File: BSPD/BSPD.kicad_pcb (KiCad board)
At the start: 4 copper layers, 53.3 x 27.9 mm, 72 parts, among them J1 Signal, J2 Power, Q1 2N7002, Q2 BSS84, Q3 2N7002, Q4 2N7002, Q5 2N7002, Q6 2N7002, U1 LM339, U2 LM339

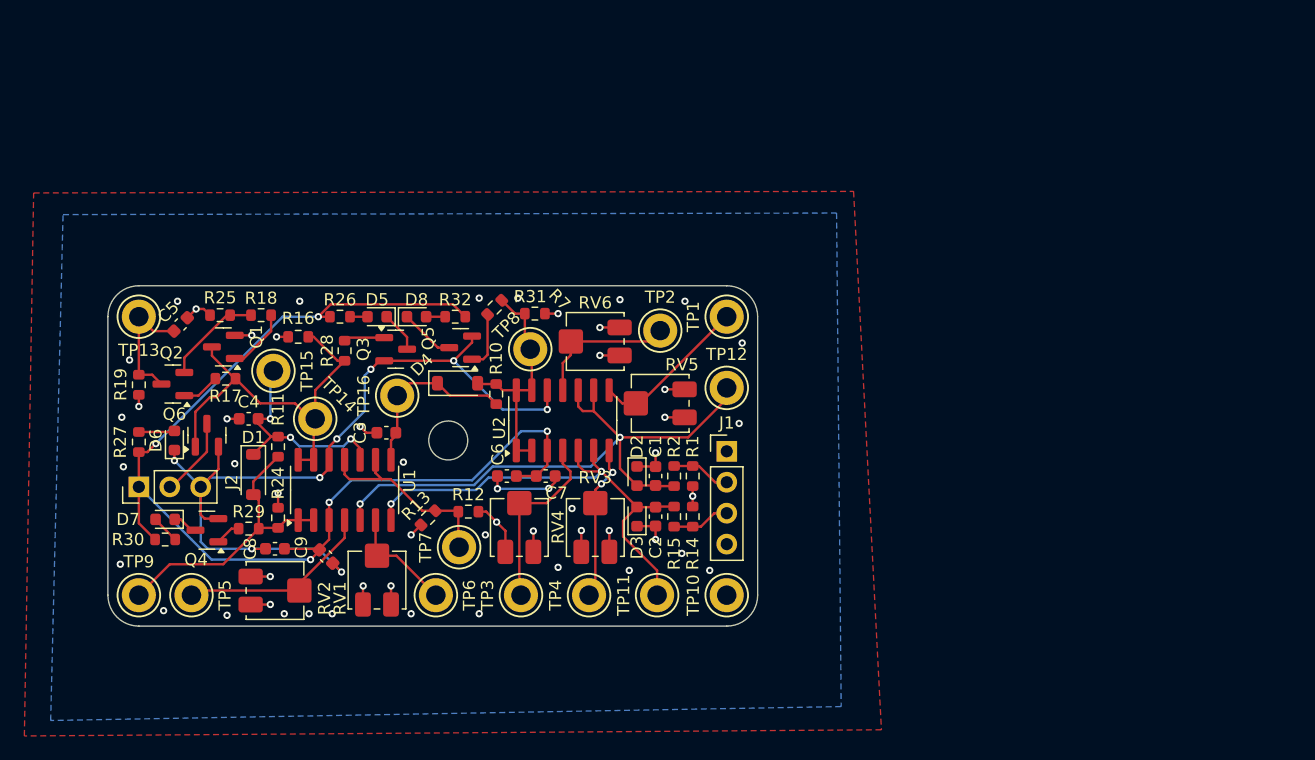
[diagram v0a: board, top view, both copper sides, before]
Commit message: feat: begin rev b
- Change parts to reduce cost (remove extended components)
- Reset PCB to prep layout
- Switch to resistor dividers
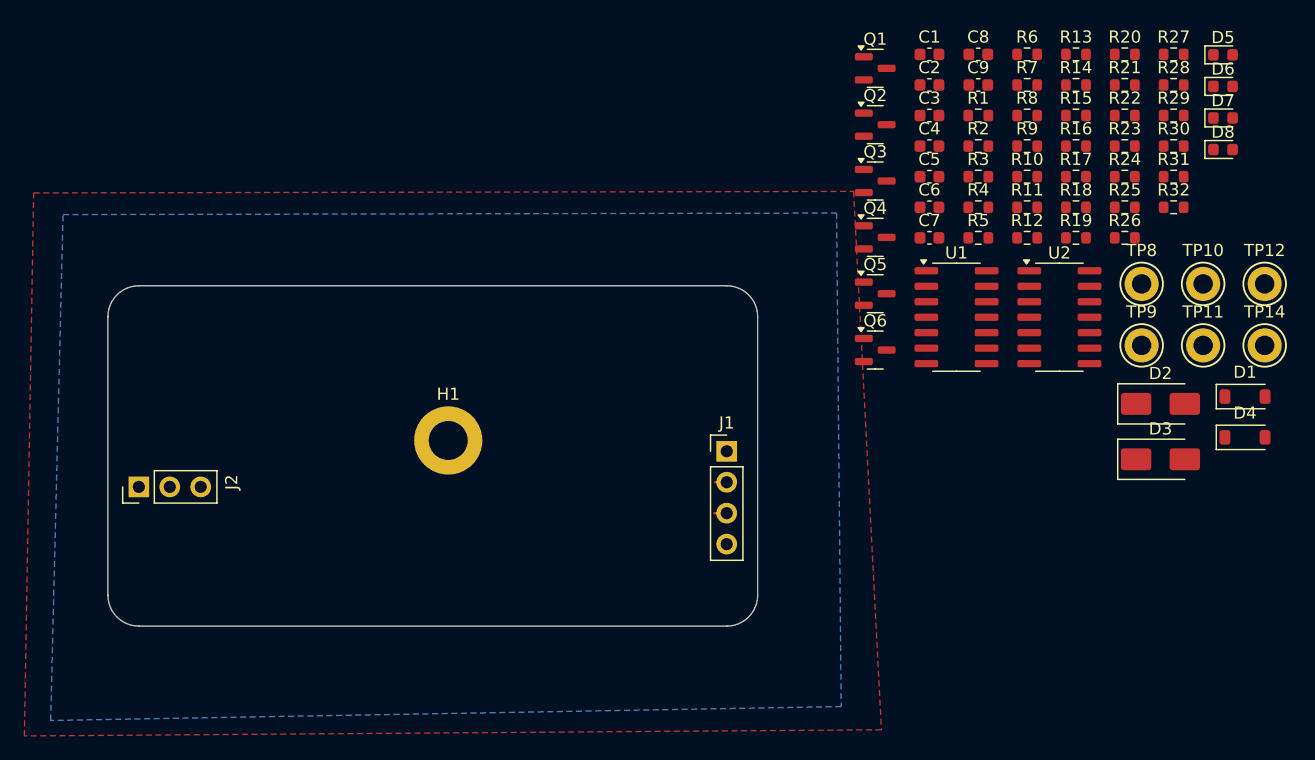
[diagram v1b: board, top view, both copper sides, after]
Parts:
- removed RV1, RV2, RV3, RV4, RV5, RV6: 3314J-1-103E, Potentiometer_SMD:Potentiometer_Bourns_3314J_Vertical
- removed TP1: TPS OV, TestPoint:TestPoint_Keystone_5005-5009_Compact
- removed TP13: Latching RC, TestPoint:TestPoint_Keystone_5005-5009_Compact
- removed TP15: ~{PANIC BRAKE} RC, TestPoint:TestPoint_Keystone_5005-5009_Compact
- removed TP16: SENSORS_OK RC, TestPoint:TestPoint_Keystone_5005-5009_Compact
- removed TP2: TPS UV, TestPoint:TestPoint_Keystone_5005-5009_Compact
- removed TP3: BPT OV, TestPoint:TestPoint_Keystone_5005-5009_Compact
- removed TP4: BPT UV, TestPoint:TestPoint_Keystone_5005-5009_Compact
- removed TP5: TPS 10%, TestPoint:TestPoint_Keystone_5005-5009_Compact
- removed TP6: BPT HB, TestPoint:TestPoint_Keystone_5005-5009_Compact
- removed TP7: TAU, TestPoint:TestPoint_Keystone_5005-5009_Compact
- added R20: 100K, Resistor_SMD:R_0603_1608Metric, F.Cu at (157.1, 29.3)
- added R21: 100K, Resistor_SMD:R_0603_1608Metric, F.Cu at (157.1, 31.8)
- added R22: 100K, Resistor_SMD:R_0603_1608Metric, F.Cu at (157.1, 34.3)
- added R23: 100K, Resistor_SMD:R_0603_1608Metric, F.Cu at (157.1, 36.8)
- added R3: 10K, Resistor_SMD:R_0603_1608Metric, F.Cu at (145.1, 39.3)
- added R4: 100K, Resistor_SMD:R_0603_1608Metric, F.Cu at (145.1, 41.8)
- added R5: 100K, Resistor_SMD:R_0603_1608Metric, F.Cu at (145.1, 44.3)
- added R6: 100K, Resistor_SMD:R_0603_1608Metric, F.Cu at (149.1, 29.3)
- added R8: 100K, Resistor_SMD:R_0603_1608Metric, F.Cu at (149.1, 34.3)
- added R9: 100K, Resistor_SMD:R_0603_1608Metric, F.Cu at (149.1, 36.8)
- C1, C2: value 150nF -> 220nF
- D1, D4: value BAT43W-V -> RB160M-30
- D2, D3: value ESDA-05N -> SMAJ5.0A; footprint Diode_SMD:D_0603_1608Metric -> Diode_SMD:D_SMA
- H1: value MountingHole -> MountingHole_Pad; footprint MountingHole:MountingHole_3.2mm_M3 -> MountingHole:MountingHole_3.2mm_M3_DIN965_Pad
- Q2: value BSS84 -> AO3401A
- R10: value 10K -> 100K
- TP9: value ~{PANIC BRAKE} -> PANIC BRAKE
- moved D7 92.9 mm to (165.2, 34.5), turned to 0 degrees
- moved D6 90.9 mm to (165.2, 31.9), turned to 0 degrees
- moved R27 90.7 mm to (161.2, 29.3), turned to 0 degrees
- moved R30 88.9 mm to (161.2, 36.8), turned to 0 degrees
- moved TP9 84.8 mm to (158.5, 53.2)
- moved R29 83.2 mm to (161.2, 34.3), turned to 0 degrees
- moved D1 81.7 mm to (167.0, 57.4), turned to 0 degrees
- moved TP14 78.2 mm to (168.6, 53.2), turned to 0 degrees
- moved R19 77.9 mm to (153.1, 44.3), turned to 0 degrees
- moved R24 74.9 mm to (157.1, 39.3), turned to 0 degrees
- moved R25 74.8 mm to (157.1, 41.8)
- moved D5 72.7 mm to (165.2, 29.3), turned to 0 degrees
- moved R17 71.8 mm to (153.1, 39.3), turned to 0 degrees
- moved R28 71.5 mm to (161.2, 31.8), turned to 0 degrees
- moved C8 70.6 mm to (145.1, 29.3), turned to 0 degrees
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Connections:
- C4 pad 1: Net-(D1-K) -> Net-(D1-A)
- C5 pad 1: Net-(Q2-D) -> Net-(Q2-S)
- D1 pad 1: Net-(D1-K) -> /PANIC_BRAKE
- D1 pad 2: /~{PANIC_BRAKE} -> Net-(D1-A)
- D2 pad 1: GNDA -> /BPT_SIG
- D2 pad 2: /TPS -> GNDA
- D3 pad 1: GNDA -> /TPS_SIG
- D3 pad 2: /BPT -> GNDA
- R10 pad 1: /SENSORS_OK -> Net-(U2A--)
- R10 pad 2: Net-(D4-K) -> GNDA
- R11 pad 1: /~{PANIC_BRAKE} -> /PANIC_BRAKE
- R11 pad 2: Net-(D1-K) -> Net-(D1-A)
- R18 pad 2: Net-(Q2-S) -> Net-(Q2-D)
- R19 pad 1: Net-(Q2-D) -> Net-(Q2-S)
- R24 pad 1: /~{PANIC_BRAKE} -> /PANIC_BRAKE
- R25 pad 2: Net-(Q2-S) -> Net-(Q2-D)
- TP9 pad 1: /~{PANIC_BRAKE} -> /PANIC_BRAKE
- U1 pad 1: /~{PANIC_BRAKE} -> /PANIC_BRAKE
- U1 pad 10: Net-(D1-K) -> Net-(D1-A)
- U1 pad 2: /~{PANIC_BRAKE} -> /PANIC_BRAKE
- U1 pad 8: Net-(D4-K) -> /1_RC
- U1 pad 9: /1_RC -> Net-(D4-K)
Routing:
- net +BATT: track 91.7 -> 0.00 mm, vias 5 -> 0
- net -BATT: track 85.7 -> 0.00 mm, vias 10 -> 0
- net /TPS: track 51.0 -> 0.00 mm, vias 2 -> 0
- net /BPT: track 41.1 -> 0.00 mm, vias 2 -> 0
- net /BSPD_OK: track 32.9 -> 0.00 mm
- net GNDA: track 26.0 -> 0.00 mm, vias 40 -> 0
- net /~{PANIC_BRAKE}: track 23.8 -> 0.00 mm
- net /SENSORS_OK: track 19.8 -> 0.00 mm
- net Net-(D1-K): track 19.5 -> 0.00 mm, vias 3 -> 0
- net /1_RC: track 16.5 -> 0.00 mm
- net Net-(U1A--): track 16.3 -> 0.00 mm
- net +5VA: track 16.0 -> 0.00 mm, vias 11 -> 0
- net Net-(U2A--): track 15.2 -> 0.00 mm
- net Net-(D4-K): track 14.7 -> 0.00 mm
- net Net-(U2D--): track 13.0 -> 0.00 mm
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
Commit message: BSPD rev 2a
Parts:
- removed D2, D3: SMAJ5.0A, Diode_SMD:D_SMA
- removed D6, D7, D8: LED, LED_SMD:LED_0603_1608Metric
- removed H1: MountingHole_Pad, MountingHole:MountingHole_3.2mm_M3_DIN965_Pad
- removed Q3, Q4, Q5: 2N7002, Package_TO_SOT_SMD:SOT-23
- removed R10, R20, R21, R22, R23, R5, R6, R8, R9: 100K, Resistor_SMD:R_0603_1608Metric
- removed R26, R27, R30, R32: 4.7K, Resistor_SMD:R_0603_1608Metric
- removed R28, R29, R31: 10K, Resistor_SMD:R_0603_1608Metric
- removed TP10: GNDA, TestPoint:TestPoint_Keystone_5005-5009_Compact
- removed TP11: BPT, TestPoint:TestPoint_Keystone_5005-5009_Compact
- removed TP12: TPS, TestPoint:TestPoint_Keystone_5005-5009_Compact
- removed TP14: BSPD OK, TestPoint:TestPoint_Keystone_5005-5009_Compact
- removed TP8: SENSORS OK, TestPoint:TestPoint_Keystone_5005-5009_Compact
- removed TP9: PANIC BRAKE, TestPoint:TestPoint_Keystone_5005-5009_Compact
- added C10: 10uF, Capacitor_SMD:C_0603_1608Metric, F.Cu at (124.2, 57.8)
- added C11: 100nF, Capacitor_SMD:C_0603_1608Metric, F.Cu at (115.4, 58.9)
- added J10: +BATT, RRM:PinHeader_1x01_P2.54mm_Circular, F.Cu at (127.0, 62.2)
- added J11: +BATT, RRM:PinHeader_1x01_P2.54mm_Circular, F.Cu at (127.0, 59.7)
- added J12: +BATT, RRM:PinHeader_1x01_P2.54mm_Circular, F.Cu at (116.8, 50.8)
- added J13: +BATT, RRM:PinHeader_1x01_P2.54mm_Circular, F.Cu at (114.3, 50.8)
- added J14: +BATT, RRM:PinHeader_1x01_P2.54mm_Circular, F.Cu at (111.8, 50.8)
- added J3: +BATT, RRM:PinHeader_1x01_P2.54mm_Circular, F.Cu at (101.6, 64.8)
- added J4: +BATT, RRM:PinHeader_1x01_P2.54mm_Circular, F.Cu at (101.6, 67.3)
- added J5: +BATT, RRM:PinHeader_1x01_P2.54mm_Circular, F.Cu at (111.8, 76.2)
- added J6: +BATT, RRM:PinHeader_1x01_P2.54mm_Circular, F.Cu at (114.3, 76.2)
- added J7: +BATT, RRM:PinHeader_1x01_P2.54mm_Circular, F.Cu at (116.8, 76.2)
- added J8: +BATT, RRM:PinHeader_1x01_P2.54mm_Circular, F.Cu at (127.0, 67.3)
- added J9: +BATT, RRM:PinHeader_1x01_P2.54mm_Circular, F.Cu at (127.0, 64.8)
- D5: value LED -> SM05; footprint LED_SMD:LED_0603_1608Metric -> Package_TO_SOT_SMD:SOT-23
- J1: value Signal -> +BATT; footprint Connector_PinHeader_2.54mm:PinHeader_1x04_P2.54mm_Vertical -> RRM:PinHeader_1x01_P2.54mm_Vertical
- J2: value Power -> +BATT; footprint Connector_PinHeader_2.54mm:PinHeader_1x03_P2.54mm_Vertical -> RRM:PinHeader_1x01_P2.54mm_Circular
- Q1, Q6: value 2N7002 -> AO3400A
- R17, R18: value 10K -> 100
- R4: value 100K -> 100
- U1, U2: footprint Package_SO:SOIC-14_3.9x8.7mm_P1.27mm -> Package_DFN_QFN:WQFN-16-1EP_3x3mm_P0.5mm_EP1.75x1.75mm
- moved R16 59.6 mm to (105.2, 72.1), turned to -90 degrees
- moved R24 59.5 mm to (108.3, 73.4), turned to 180 degrees
- moved R25 56.8 mm to (105.5, 65.7)
- moved D1 56.4 mm to (112.5, 71.8), turned to 90 degrees
- moved D5 53.7 mm to (123.7, 63.4), turned to 180 degrees
- moved R18 52.5 mm to (107.7, 68.1), turned to 90 degrees
- moved R13 52.2 mm to (123.3, 72.1)
- moved D4 51.7 mm to (115.6, 66.9), turned to 90 degrees
- moved R17 51.0 mm to (111.0, 68.1), turned to 45 degrees
- moved Q1 49.5 mm to (105.0, 68.5), turned to -90 degrees
- moved R11 49.3 mm to (110.6, 72.6), turned to 90 degrees
- moved C8 48.7 mm to (119.4, 70.6), turned to 90 degrees
- moved C4 48.0 mm to (108.3, 71.9), turned to 180 degrees
- moved C9 45.8 mm to (120.9, 70.6), turned to 90 degrees
- moved R14 45.4 mm to (124.1, 66.7), turned to -90 degrees
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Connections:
- net Net-(Q2-D) renamed /BSPD_RST
- D5 pad 1: Net-(D5-K) -> /BPT_SIG
- D5 pad 2: Net-(D5-A) -> /TPS_SIG
- J1 pad 1: +5VA -> +BATT
- J2 pad 1: +BATT -> /BSPD_SD-
- Q1 pad 2: GNDA -> -BATT
- Q6 pad 1: /BSPD_OK -> Net-(Q6-G)
- R25 pad 1: GNDA -> -BATT
- R4 pad 1: Net-(U2C-+) -> /BSPD_OK
- R4 pad 2: Net-(U2D--) -> Net-(Q6-G)
- U1 pad 1: /PANIC_BRAKE -> +BATT
- U1 pad 10: Net-(D1-A) -> unconnected-(U1E-NC-Pad10)
- U1 pad 11: /1_RC -> Net-(D4-K)
- U1 pad 2: /PANIC_BRAKE -> /BPT_HB_TH
- U1 pad 3: +BATT -> unconnected-(U1E-NC-Pad3)
- U1 pad 4: Net-(U1A--) -> /BPT
- U1 pad 5: /TPS -> /TPS_HB_TH
- U1 pad 6: Net-(U1B--) -> /TPS
- U1 pad 7: /BPT -> Net-(D1-A)
- U1 pad 9: Net-(D4-K) -> /1_RC
- U2 pad 1: /SENSORS_OK -> +BATT
- U2 pad 10: /TPS -> unconnected-(U2E-NC-Pad10)
- U2 pad 11: Net-(U2C-+) -> /TPS_MAX_TH
- U2 pad 2: /SENSORS_OK -> /BPT_MIN_TH
- U2 pad 3: +BATT -> unconnected-(U2E-NC-Pad3)
- U2 pad 4: Net-(U2A--) -> /BPT
- U2 pad 6: /BPT -> /BPT_MAX_TH
- U2 pad 7: Net-(U2B-+) -> /TPS_MIN_TH
- U2 pad 8: Net-(U2D--) -> /TPS
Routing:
- net +BATT: track 0.00 -> 58.1 mm, vias 0 -> 5
- net -BATT: track 0.00 -> 42.3 mm, vias 0 -> 5
- net /TPS_HB_TH: track 0.00 -> 26.0 mm, vias 0 -> 2
- net /BSPD_OK: track 0.00 -> 21.0 mm
- net /BPT_MAX_TH: track 0.00 -> 20.8 mm, vias 0 -> 1
- net /BPT: track 0.00 -> 20.0 mm, vias 0 -> 2
- net /TPS: track 0.00 -> 19.6 mm, vias 0 -> 2
- net /TPS_MIN_TH: track 0.00 -> 14.5 mm, vias 0 -> 2
- net /TPS_MAX_TH: track 0.00 -> 14.4 mm
- net /BPT_MIN_TH: track 0.00 -> 13.9 mm, vias 0 -> 1
- net Net-(D1-A): track 0.00 -> 13.2 mm, vias 0 -> 2
- net +5VA: track 0.00 -> 10.7 mm, vias 0 -> 4
- net /BSPD_RST: track 0.00 -> 10.7 mm, vias 0 -> 1
- net /SENSORS_OK: track 0.00 -> 9.74 mm
- net /1_RC: track 0.00 -> 8.90 mm
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- added copper zone on In2.Cu, net +5VA
- added copper zone on F.Cu, net -BATT
- added copper zone on In1.Cu, net GNDA
- removed copper zone on In1.Cu, net +5VA
- removed copper zone on In2.Cu, net GNDA
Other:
- board size 53.3 x 27.9 mm -> 30.5 x 30.5 mm
- board text added: "RRM BSPD Module A1"
- board text added: "Race Ready Modules BSPD Module Rev. A1"
